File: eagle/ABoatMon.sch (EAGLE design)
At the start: 29 parts, among them J1 VUSB, J2 GND, J3 GND, X1 MKDSN1,5/2-5,08

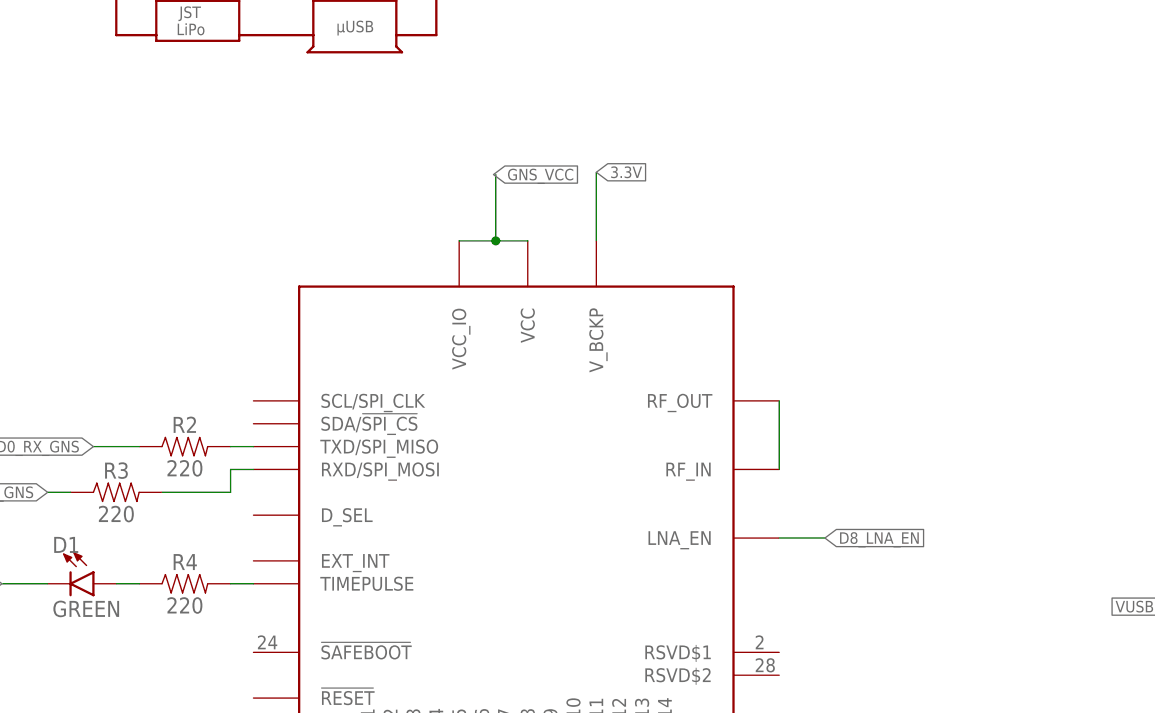
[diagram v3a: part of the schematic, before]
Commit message: changed nets for gns
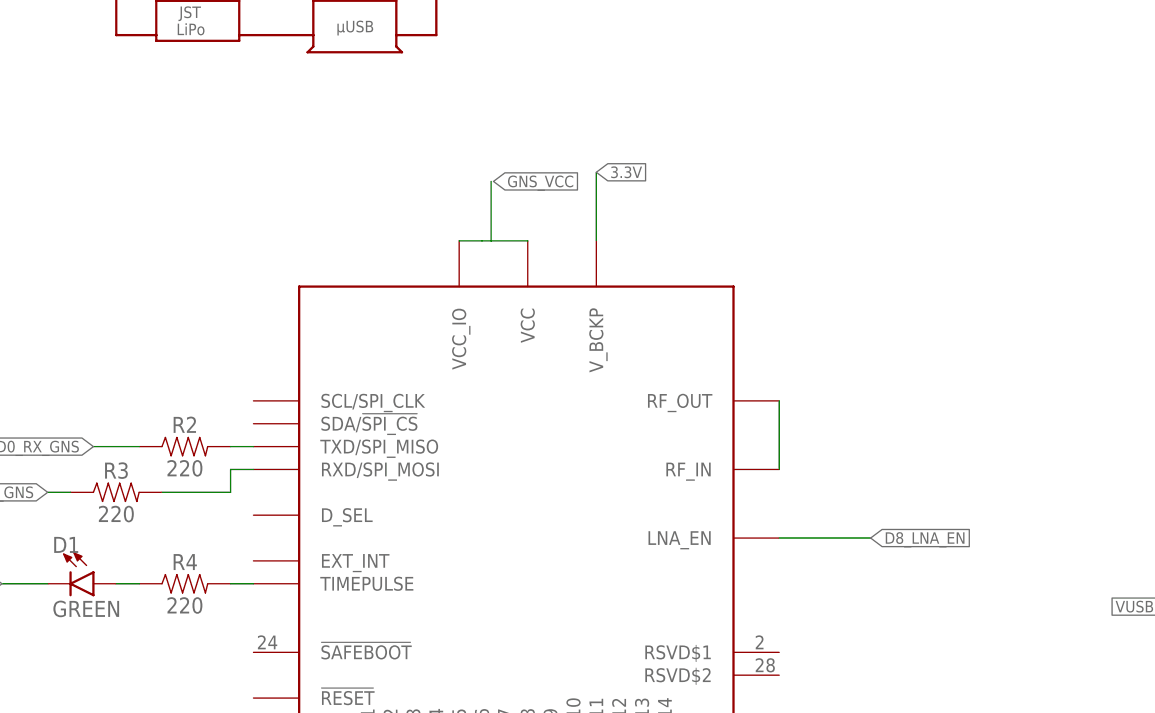
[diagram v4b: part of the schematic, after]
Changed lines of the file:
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@@
 <clearance class="1" value="0.4064"/>
+</class>
+<class number="2" name="gns" width="0" drill="0">
 </class>
 </classes>
@@
 </segment>
 </net>
-<net name="3.3V" class="1">
+<net name="3.3V" class="2">
 <segment>
 <pinref part="U$6" gate="G$1" pin="3V3"/>
@@
 </segment>
 </net>
-<net name="D8_LNA_EN" class="0">
-<segment>
-<pinref part="U$5" gate="G$1" pin="LNA_EN"/>
-<wire x1="111.76" y1="50.8" x2="116.84" y2="50.8" width="0.1524" layer="91"/>
-<label x="116.84" y="50.8" size="1.27" layer="95" xref="yes"/>
-</segment>
+<net name="D8_LNA_EN" class="2">
 <segment>
 <pinref part="U$6" gate="G$1" pin="D8"/>
@@
 <label x="86.36" y="157.48" size="1.27" layer="95" xref="yes"/>
 </segment>
-</net>
-<net name="N$2" class="0">
-<segment>
-<pinref part="R2" gate="G$1" pin="2"/>
-<pinref part="U$5" gate="G$1" pin="TXD/SPI_MISO"/>
-<wire x1="50.8" y1="60.96" x2="53.34" y2="60.96" width="0.1524" layer="91"/>
-</segment>
-</net>
-<net name="N$3" class="0">
-<segment>
-<pinref part="R3" gate="G$1" pin="2"/>
-<wire x1="43.18" y1="55.88" x2="50.8" y2="55.88" width="0.1524" layer="91"/>
-<wire x1="50.8" y1="55.88" x2="50.8" y2="58.42" width="0.1524" layer="91"/>
-<pinref part="U$5" gate="G$1" pin="RXD/SPI_MOSI"/>
-<wire x1="50.8" y1="58.42" x2="53.34" y2="58.42" width="0.1524" layer="91"/>
+<segment>
+<pinref part="U$5" gate="G$1" pin="LNA_EN"/>
+<wire x1="111.76" y1="50.8" x2="121.92" y2="50.8" width="0.1524" layer="91"/>
+<label x="121.92" y="50.8" size="1.27" layer="95" xref="yes"/>
 </segment>
 </net>
@@
 </segment>
 </net>
-<net name="GNS_VCC" class="1">
+<net name="GNS_VCC" class="2">
 <segment>
 <pinref part="C3" gate="G$1" pin="1"/>
@@
 <pinref part="U$5" gate="G$1" pin="VCC_IO"/>
 <pinref part="U$5" gate="G$1" pin="VCC"/>
-<wire x1="76.2" y1="83.82" x2="80.264" y2="83.82" width="0.1524" layer="91"/>
-<label x="80.01" y="91.186" size="1.27" layer="95" xref="yes"/>
-<wire x1="80.264" y1="83.82" x2="83.82" y2="83.82" width="0.1524" layer="91"/>
-<wire x1="80.264" y1="91.186" x2="80.264" y2="83.82" width="0.1524" layer="91"/>
-<junction x="80.264" y="83.82"/>
-</segment>
-</net>
+<wire x1="76.2" y1="83.82" x2="78.74" y2="83.82" width="0.1524" layer="91"/>
+<wire x1="79.756" y1="83.82" x2="83.82" y2="83.82" width="0.1524" layer="91"/>
+<wire x1="78.74" y1="83.82" x2="79.756" y2="83.82" width="0.1524" layer="91"/>
+<wire x1="79.756" y1="83.82" x2="79.756" y2="90.424" width="0.1524" layer="91"/>
+<label x="80.01" y="90.424" size="1.27" layer="95" xref="yes"/>
+</segment>
+</net>
+<net name="N$3" class="2">
+<segment>
+<pinref part="U$5" gate="G$1" pin="RXD/SPI_MOSI"/>
+<wire x1="53.34" y1="58.42" x2="50.8" y2="58.42" width="0.1524" layer="91"/>
+<wire x1="50.8" y1="58.42" x2="50.8" y2="55.88" width="0.1524" layer="91"/>
+<pinref part="R3" gate="G$1" pin="2"/>
+<wire x1="50.8" y1="55.88" x2="43.18" y2="55.88" width="0.1524" layer="91"/>
+</segment>
+</net>
+<net name="N$2" class="2">
+<segment>
+<pinref part="U$5" gate="G$1" pin="TXD/SPI_MISO"/>
+<pinref part="R2" gate="G$1" pin="2"/>
+<wire x1="53.34" y1="60.96" x2="50.8" y2="60.96" width="0.1524" layer="91"/>
+</segment>
+</net>

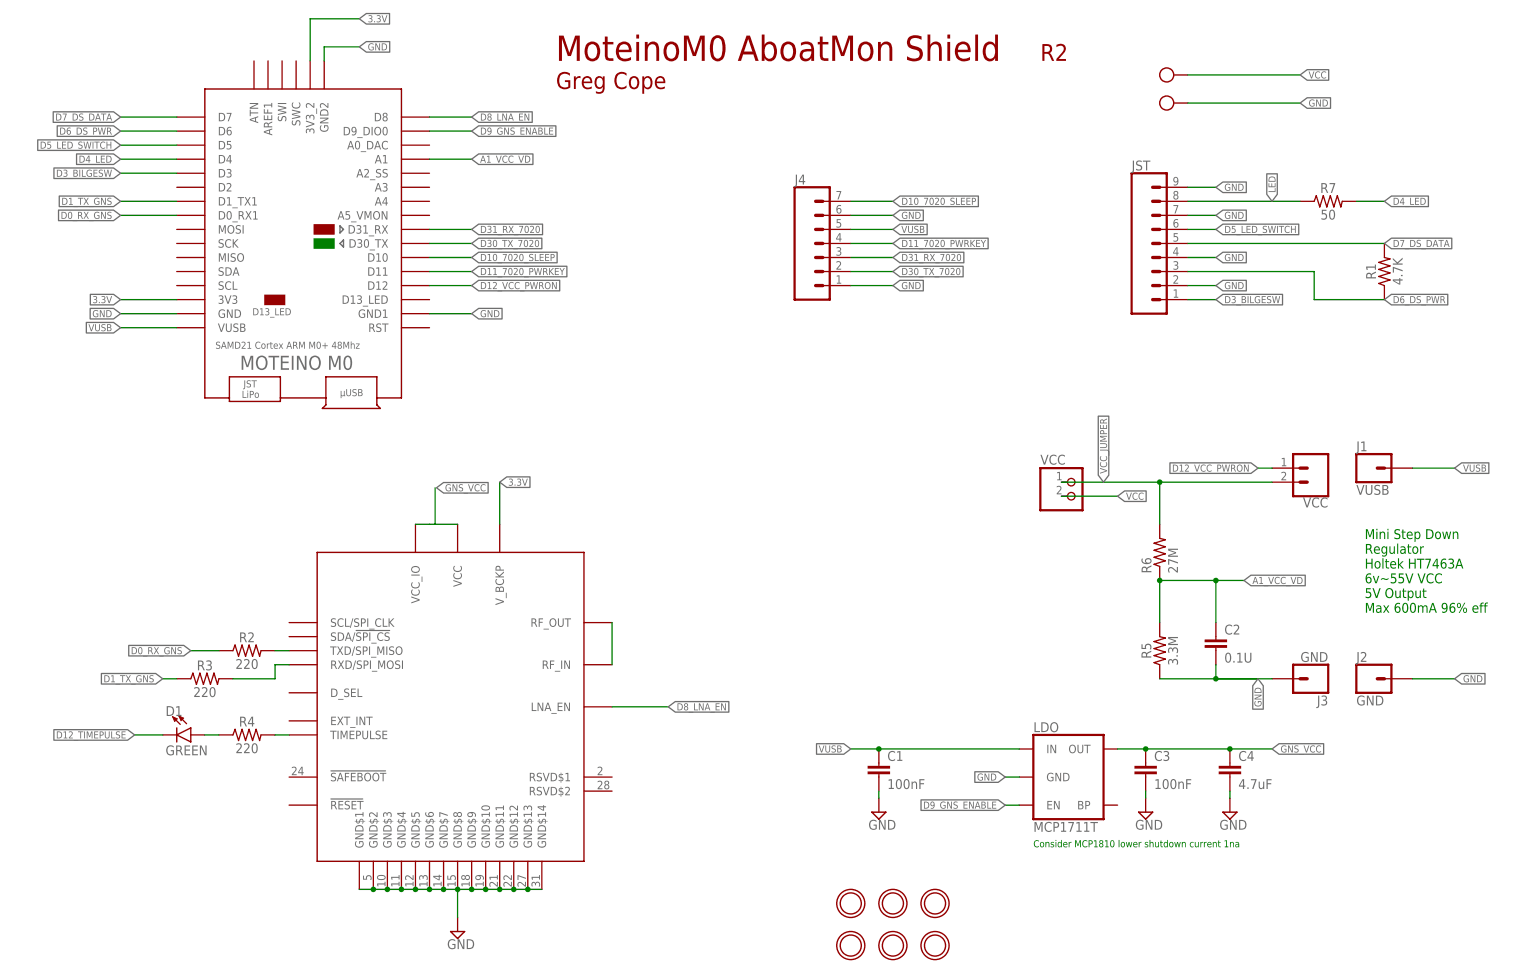
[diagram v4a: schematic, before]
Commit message: first pass with vias - one airwire
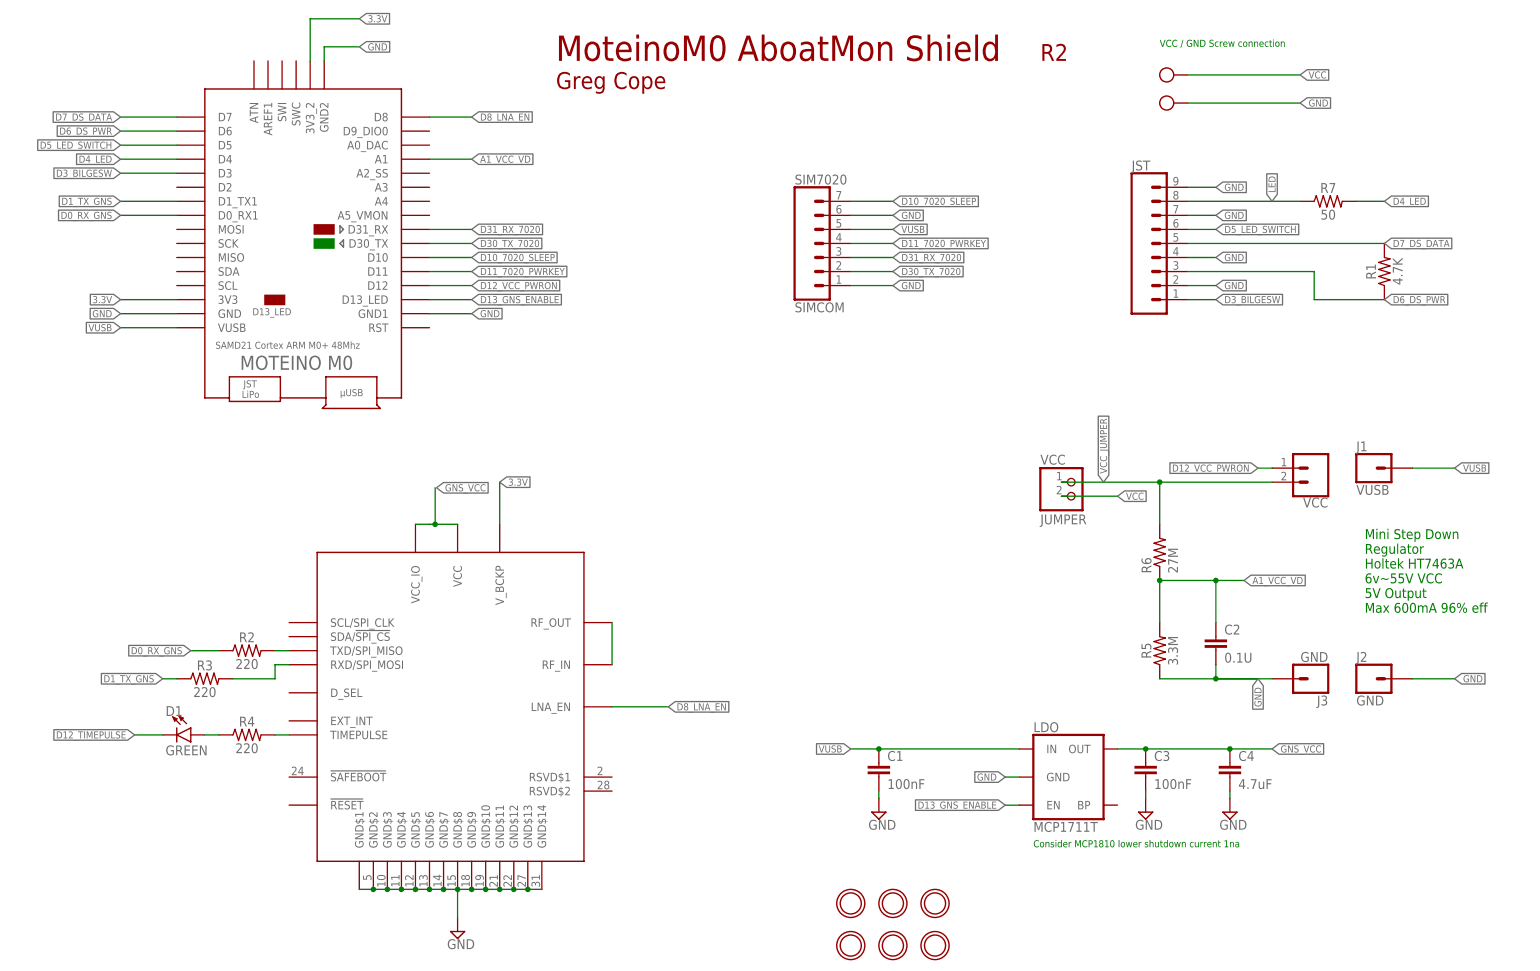
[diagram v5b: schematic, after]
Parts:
- SIM7020: value (none) -> SIMCOM
- VCC: value (none) -> JUMPER
- renumbered J4 to SIM7020
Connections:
- removed net D9_GNS_ENABLE: LDO.EN, U$6.D9_DIO0
- new net D13_GNS_ENABLE: LDO.EN, U$6.D13_LED
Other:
- note added: "VCC / GND Screw connection"
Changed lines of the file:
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@@
 </variantdefs>
 <classes>
-<class number="0" name="default" width="0.6096" drill="0">
-<clearance class="0" value="0.4064"/>
+<class number="0" name="default" width="0.4572" drill="0">
+<clearance class="0" value="0.3048"/>
 </class>
 <class number="1" name="power" width="0.6096" drill="0">
@@
 <part name="U$2" library="microbuilder" deviceset="MOUNTINGHOLE" device="2.5"/>
 <part name="U$4" library="microbuilder" deviceset="MOUNTINGHOLE" device="2.5"/>
-<part name="VCC" library="microbuilder" deviceset="HEADER-1X2" device="ROUND"/>
+<part name="VCC" library="microbuilder" deviceset="HEADER-1X2" device="ROUND" value="JUMPER"/>
 <part name="U$1" library="microbuilder" deviceset="MOUNTINGHOLE" device="2.5"/>
 <part name="GND" library="microbuilder" deviceset="MOUNTINGHOLE" device="2.5"/>
@@
 <part name="SUPPLY5" library="supply2" library_urn="urn:adsk.eagle:library:372" deviceset="GND" device=""/>
 <part name="D1" library="SparkFun-LED" library_urn="urn:adsk.eagle:library:529" deviceset="LED-GREEN" device="0603" package3d_urn="urn:adsk.eagle:package:39354/1" value="GREEN"/>
-<part name="J4" library="SparkFun-Connectors" library_urn="urn:adsk.eagle:library:513" deviceset="CONN_07" device="" package3d_urn="urn:adsk.eagle:package:38129/1"/>
+<part name="SIM7020" library="SparkFun-Connectors" library_urn="urn:adsk.eagle:library:513" deviceset="CONN_07" device="" package3d_urn="urn:adsk.eagle:package:38129/1" value="SIMCOM"/>
 </parts>
 <sheets>
@@
 <text x="101.6" y="167.64" size="4.572" layer="94" ratio="15">MoteinoM0 AboatMon Shield</text>
 <text x="187.96" y="25.4" size="1.27" layer="91">Consider MCP1810 lower shutdown current 1na</text>
+<text x="210.82" y="170.18" size="1.27" layer="91">VCC / GND Screw connection</text>
 </plain>
 <instances>
@@
 <attribute name="VALUE" x="30.988" y="43.815" size="1.778" layer="96" font="vector" align="top-left"/>
 </instance>
-<instance part="J4" gate="G$1" x="149.86" y="132.08" smashed="yes">
+<instance part="SIM7020" gate="G$1" x="149.86" y="132.08" smashed="yes">
 <attribute name="VALUE" x="144.78" y="122.174" size="1.778" layer="96" font="vector"/>
 <attribute name="NAME" x="144.78" y="145.288" size="1.778" layer="95" font="vector"/>
@@
 </segment>
 <segment>
-<pinref part="J4" gate="G$1" pin="1"/>
+<pinref part="SIM7020" gate="G$1" pin="1"/>
 <wire x1="154.94" y1="127" x2="162.56" y2="127" width="0.1524" layer="91"/>
 <label x="162.56" y="127" size="1.27" layer="95" xref="yes"/>
 </segment>
 <segment>
-<pinref part="J4" gate="G$1" pin="6"/>
+<pinref part="SIM7020" gate="G$1" pin="6"/>
 <wire x1="154.94" y1="139.7" x2="162.56" y2="139.7" width="0.1524" layer="91"/>
 <label x="162.56" y="139.7" size="1.27" layer="95" xref="yes"/>
@@
 </segment>
 <segment>
-<pinref part="J4" gate="G$1" pin="5"/>
+<pinref part="SIM7020" gate="G$1" pin="5"/>
 <wire x1="154.94" y1="137.16" x2="162.56" y2="137.16" width="0.1524" layer="91"/>
 <label x="162.56" y="137.16" size="1.27" layer="95" xref="yes"/>
@@
 </segment>
 <segment>
-<pinref part="J4" gate="G$1" pin="2"/>
+<pinref part="SIM7020" gate="G$1" pin="2"/>
 <wire x1="154.94" y1="129.54" x2="162.56" y2="129.54" width="0.1524" layer="91"/>
 <label x="162.56" y="129.54" size="1.27" layer="95" xref="yes"/>
@@
 <pinref part="R1" gate="G$1" pin="2"/>
 <label x="251.46" y="134.62" size="1.27" layer="95" xref="yes"/>
-</segment>
-</net>
-<net name="D9_GNS_ENABLE" class="0">
-<segment>
-<pinref part="U$6" gate="G$1" pin="D9_DIO0"/>
-<wire x1="78.74" y1="154.94" x2="86.36" y2="154.94" width="0.1524" layer="91"/>
-<label x="86.36" y="154.94" size="1.27" layer="95" xref="yes"/>
-</segment>
-<segment>
-<pinref part="LDO" gate="G$1" pin="EN"/>
-<wire x1="185.42" y1="33.02" x2="182.88" y2="33.02" width="0.1524" layer="91"/>
-<label x="182.88" y="33.02" size="1.27" layer="95" rot="R180" xref="yes"/>
 </segment>
 </net>
@@
 </segment>
 <segment>
-<pinref part="J4" gate="G$1" pin="3"/>
+<pinref part="SIM7020" gate="G$1" pin="3"/>
 <wire x1="154.94" y1="132.08" x2="162.56" y2="132.08" width="0.1524" layer="91"/>
 <label x="162.56" y="132.08" size="1.27" layer="95" xref="yes"/>
@@
 </segment>
 <segment>
-<pinref part="J4" gate="G$1" pin="7"/>
+<pinref part="SIM7020" gate="G$1" pin="7"/>
 <wire x1="154.94" y1="142.24" x2="162.56" y2="142.24" width="0.1524" layer="91"/>
 <label x="162.56" y="142.24" size="1.27" layer="95" xref="yes"/>
@@
 </segment>
 <segment>
-<pinref part="J4" gate="G$1" pin="4"/>
+<pinref part="SIM7020" gate="G$1" pin="4"/>
 <wire x1="154.94" y1="134.62" x2="162.56" y2="134.62" width="0.1524" layer="91"/>
 <label x="162.56" y="134.62" size="1.27" layer="95" xref="yes"/>
@@
 <wire x1="79.756" y1="83.82" x2="79.756" y2="90.424" width="0.1524" layer="91"/>
 <label x="80.01" y="90.424" size="1.27" layer="95" xref="yes"/>
+<junction x="79.756" y="83.82"/>
 </segment>
 </net>
@@
 </segment>
 </net>
+<net name="D13_GNS_ENABLE" class="0">
+<segment>
+<pinref part="LDO" gate="G$1" pin="EN"/>
+<wire x1="185.42" y1="33.02" x2="182.88" y2="33.02" width="0.1524" layer="91"/>
+<label x="182.88" y="33.02" size="1.27" layer="95" rot="R180" xref="yes"/>
+</segment>
+<segment>
+<pinref part="U$6" gate="G$1" pin="D13_LED"/>
+<wire x1="78.74" y1="124.46" x2="86.36" y2="124.46" width="0.1524" layer="91"/>
+<label x="86.36" y="124.46" size="1.27" layer="95" xref="yes"/>
+</segment>
+</net>

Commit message: added tab
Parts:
- added J4: LIPO, SparkFun-Connectors:CONN_01
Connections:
- new net LIPO: C1.1, J4.1, LDO.IN, SIM7020.5
- net 3.3V: no longer U$6.3V3, U$6.3V3_2
- net VUSB: no longer C1.1, LDO.IN, SIM7020.5
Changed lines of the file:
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@@
 <part name="D1" library="SparkFun-LED" library_urn="urn:adsk.eagle:library:529" deviceset="LED-GREEN" device="0603" package3d_urn="urn:adsk.eagle:package:39354/1" value="GREEN"/>
 <part name="SIM7020" library="SparkFun-Connectors" library_urn="urn:adsk.eagle:library:513" deviceset="CONN_07" device="" package3d_urn="urn:adsk.eagle:package:38129/1" value="SIMCOM"/>
+<part name="J4" library="SparkFun-Connectors" deviceset="CONN_01" device="" value="LIPO"/>
 </parts>
 <sheets>
@@
 <attribute name="VALUE" x="144.78" y="122.174" size="1.778" layer="96" font="vector"/>
 <attribute name="NAME" x="144.78" y="145.288" size="1.778" layer="95" font="vector"/>
+</instance>
+<instance part="J4" gate="G$1" x="144.78" y="43.18" smashed="yes">
+<attribute name="VALUE" x="142.24" y="38.354" size="1.778" layer="96" font="vector"/>
+<attribute name="NAME" x="142.24" y="46.228" size="1.778" layer="95" font="vector"/>
 </instance>
 </instances>
@@
 <label x="264.16" y="93.98" size="1.27" layer="95" xref="yes"/>
 </segment>
-<segment>
-<pinref part="LDO" gate="G$1" pin="IN"/>
-<pinref part="C1" gate="G$1" pin="1"/>
-<wire x1="185.42" y1="43.18" x2="160.02" y2="43.18" width="0.1524" layer="91"/>
-<wire x1="160.02" y1="43.18" x2="154.94" y2="43.18" width="0.1524" layer="91"/>
-<junction x="160.02" y="43.18"/>
-<label x="154.94" y="43.18" size="1.27" layer="95" rot="R180" xref="yes"/>
-</segment>
-<segment>
-<pinref part="SIM7020" gate="G$1" pin="5"/>
-<wire x1="154.94" y1="137.16" x2="162.56" y2="137.16" width="0.1524" layer="91"/>
-<label x="162.56" y="137.16" size="1.27" layer="95" xref="yes"/>
-</segment>
 </net>
 <net name="3.3V" class="2">
-<segment>
-<pinref part="U$6" gate="G$1" pin="3V3"/>
-<wire x1="33.02" y1="124.46" x2="22.86" y2="124.46" width="0.1524" layer="91"/>
-<label x="22.86" y="124.46" size="1.27" layer="95" rot="R180" xref="yes"/>
-</segment>
-<segment>
-<pinref part="U$6" gate="G$1" pin="3V3_2"/>
-<wire x1="57.15" y1="167.64" x2="57.15" y2="175.26" width="0.1524" layer="91"/>
-<wire x1="57.15" y1="175.26" x2="66.04" y2="175.26" width="0.1524" layer="91"/>
-<label x="66.04" y="175.26" size="1.27" layer="95" xref="yes"/>
-</segment>
 <segment>
 <pinref part="U$5" gate="G$1" pin="V_BCKP"/>
@@
 </segment>
 </net>
+<net name="LIPO" class="0">
+<segment>
+<pinref part="LDO" gate="G$1" pin="IN"/>
+<pinref part="C1" gate="G$1" pin="1"/>
+<wire x1="185.42" y1="43.18" x2="160.02" y2="43.18" width="0.1524" layer="91"/>
+<wire x1="160.02" y1="43.18" x2="152.4" y2="43.18" width="0.1524" layer="91"/>
+<junction x="160.02" y="43.18"/>
+<pinref part="J4" gate="G$1" pin="1"/>
+</segment>
+<segment>
+<pinref part="SIM7020" gate="G$1" pin="5"/>
+<wire x1="154.94" y1="137.16" x2="162.56" y2="137.16" width="0.1524" layer="91"/>
+<label x="162.56" y="137.16" size="1.27" layer="95" xref="yes"/>
+</segment>
+</net>
